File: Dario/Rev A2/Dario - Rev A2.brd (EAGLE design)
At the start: 55 x 30 mm, 31 parts, among them J1 1241050-5, J2 21_PIN, J3 21_PIN, SW1 KMR211G, U1 MK20DX256VLH7, Y1 8MHz, Y2 32.768kHz, 12.5pF

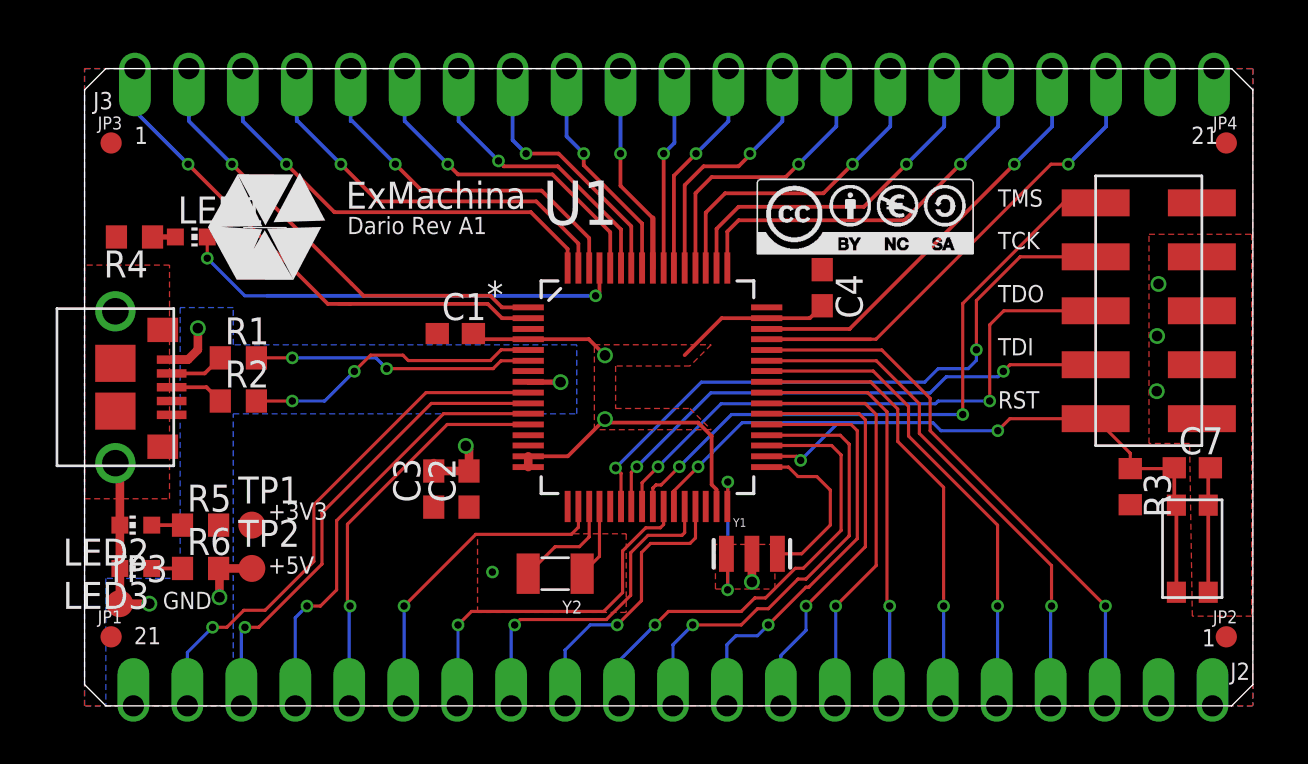
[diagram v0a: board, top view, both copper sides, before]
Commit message: Change the pin out of the jtag connector and change the width of all nets to 0.1778mm
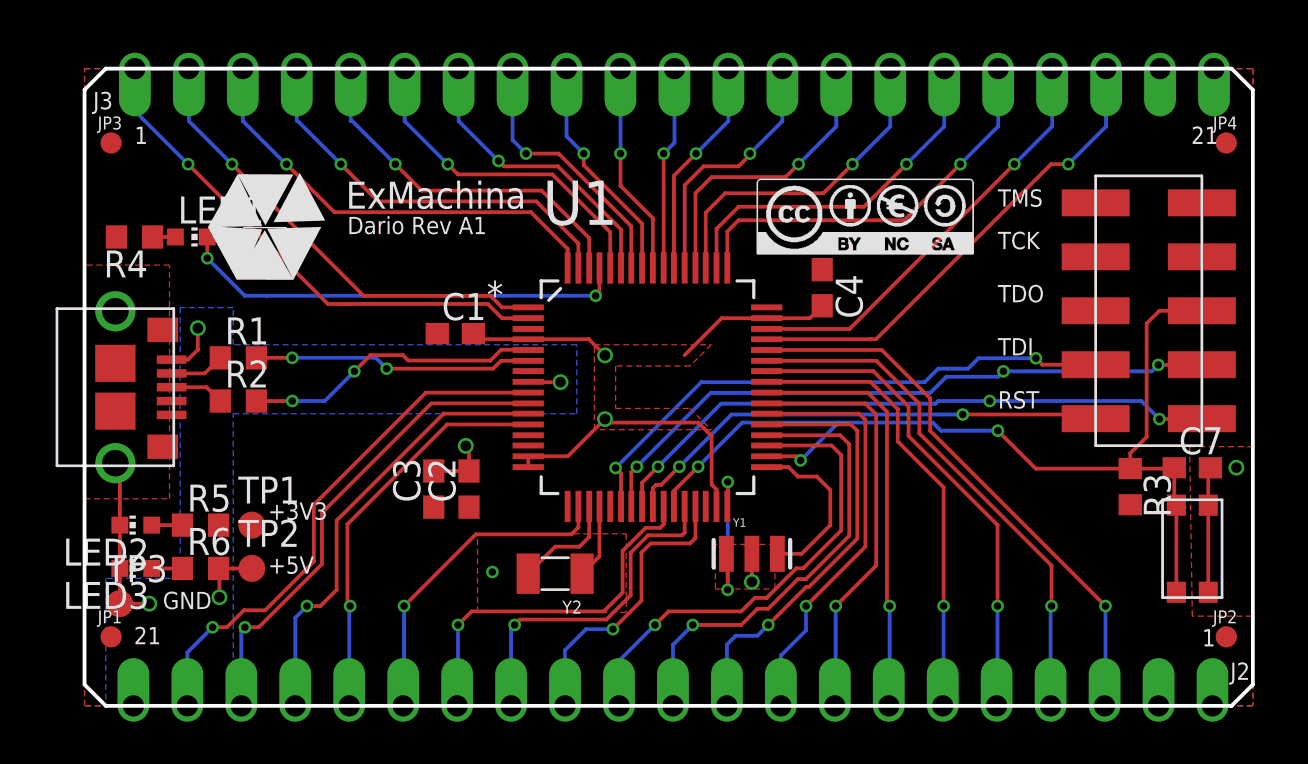
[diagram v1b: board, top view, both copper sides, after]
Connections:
- net GND: now also J1.2; no longer J1.3, J1.5, J1.7, J1.9
- net RESET: now also J1.5; no longer J1.10
- net TCK/SWDCLK: now also J1.8; no longer J1.4
- net TDI: now also J1.7; no longer J1.8
- net TDO: now also J1.9; no longer J1.6
- net TMS/SWDIO: now also J1.10; no longer J1.2
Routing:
- net RESET: track 37.5 -> 46.6 mm
- net TMS/SWDIO: track 30.4 -> 23.3 mm
- net TDI: track 25.6 -> 30.6 mm, vias 2 -> 3
- net TCK/SWDCLK: track 30.3 -> 26.8 mm
- net TDO: track 27.9 -> 29.4 mm, vias 2 -> 3
- net GND: vias 9 -> 7

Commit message: Enlarge the board to have a multiple of 0.1 inch
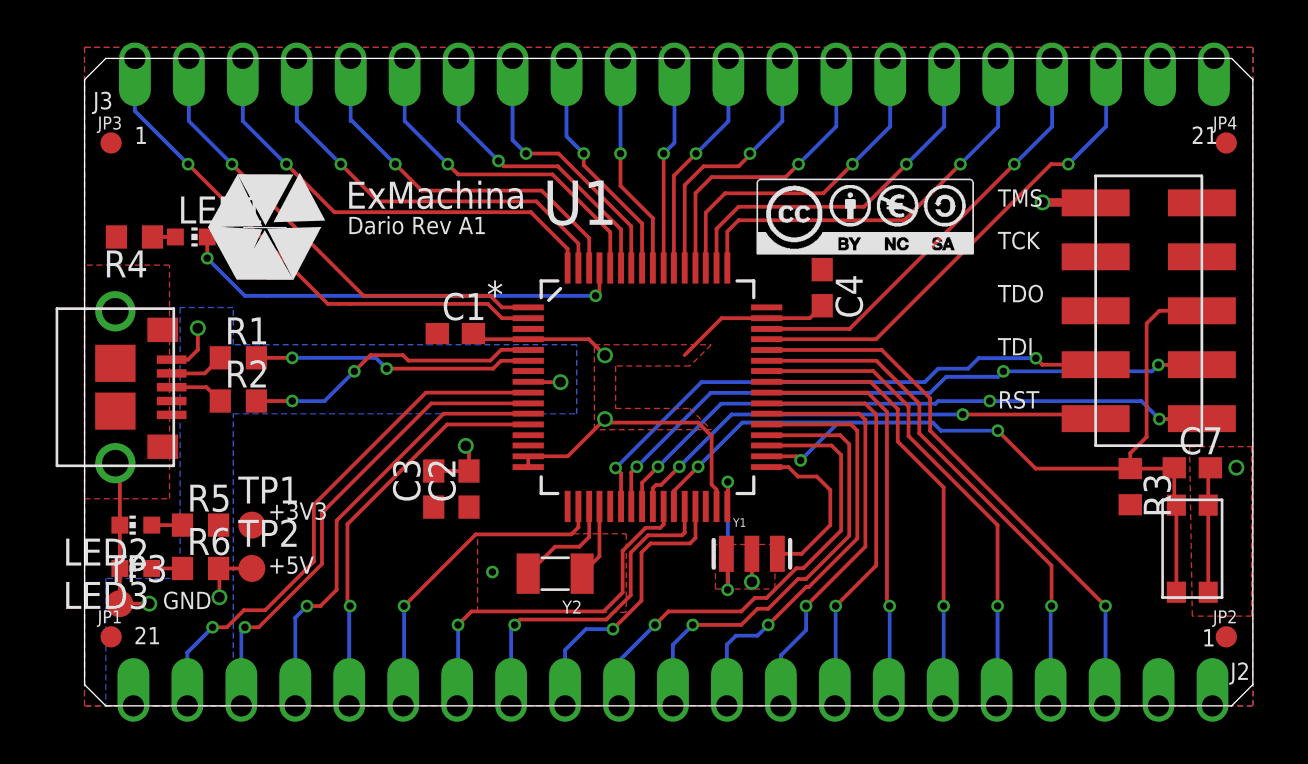
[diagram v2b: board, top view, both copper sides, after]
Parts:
- moved J3 0.48 mm to (27.8, 30.5)
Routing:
- net GND: track 46.3 -> 48.8 mm, vias 7 -> 8
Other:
- board size 55 x 30 mm -> 55 x 30.5 mm

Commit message: Rename the name on the board and add the name on some pin of JTAG connector
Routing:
- net TDO: vias 3 -> 2
- net TDI: vias 3 -> 2
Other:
- outline, holes or cut-outs redrawn
- board text removed: "RST"
- board text removed: "TDI"
- board text removed: "TDO"
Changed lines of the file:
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@@
 <setting verticaltext="up"/>
 </settings>
-<grid distance="0.1" unitdist="inch" unit="mm" style="lines" multiple="1" display="yes" altdistance="0.05" altunitdist="inch" altunit="mm"/>
+<grid distance="1.27" unitdist="mm" unit="mm" style="lines" multiple="1" display="yes" altdistance="0.635" altunitdist="mm" altunit="mm"/>
 <layers>
 <layer number="1" name="Top" color="4" fill="1" visible="yes" active="yes"/>
@@
 <wire x1="54" y1="30.48" x2="1" y2="30.48" width="0" layer="20"/>
 <wire x1="1" y1="30.48" x2="0" y2="29.48" width="0" layer="20"/>
-<wire x1="0" y1="29.48" x2="0" y2="29" width="0" layer="20"/>
-<wire x1="0" y1="29" x2="0" y2="1" width="0" layer="20"/>
+<wire x1="0" y1="29.48" x2="0" y2="1" width="0" layer="20"/>
 <wire x1="0" y1="1" x2="1" y2="0" width="0" layer="20"/>
 <wire x1="1" y1="0" x2="54" y2="0" width="0" layer="20"/>
@@
 <text x="0.402" y="28.086" size="0.8128" layer="21">J3</text>
 <text x="53.934" y="1.222" size="0.8128" layer="21">J2</text>
-<text x="43" y="14" size="0.8128" layer="21">RST</text>
-<text x="43" y="16.5" size="0.8128" layer="21">TDI</text>
-<text x="43" y="19" size="0.8128" layer="21">TDO</text>
-<text x="43" y="23.5" size="0.8128" layer="21">TMS</text>
-<text x="43" y="21.5" size="0.8128" layer="21">TCK</text>
+<text x="43" y="23.5" size="0.8128" layer="21">GND</text>
+<text x="41.73" y="15.785" size="0.8128" layer="21">TCK</text>
+<text x="41.73" y="13.975" size="0.8128" layer="21">TMS</text>
 </plain>
 <attributes>
@@
 <via x="19.2" y="6.3" extent="1-16" drill="0.35"/>
 <contactref element="J1" pad="2"/>
-<via x="45.1" y="23.7" extent="1-16" drill="0.5"/>
+<via x="50.18" y="23.7" extent="1-16" drill="0.5"/>
 <wire x1="47.6" y1="23.68" x2="47.58" y2="23.7" width="0.4064" layer="1"/>
-<wire x1="47.58" y1="23.7" x2="45.1" y2="23.7" width="0.4064" layer="1"/>
+<wire x1="47.58" y1="23.7" x2="50.18" y2="23.7" width="0.4064" layer="1"/>
 </signal>
 <signal name="+5V">
@@
 <wire x1="26.246" y1="9.3866" x2="26.246" y2="10.503" width="0.1778" layer="1"/>
 <wire x1="26.246" y1="10.503" x2="27" y2="11.257" width="0.1778" layer="1"/>
-<via x="42.612" y="14.351" extent="1-16" drill="0.35"/>
 <wire x1="29.967" y1="14.224" x2="40.061" y2="14.224" width="0.1778" layer="16"/>
 <wire x1="40.061" y1="14.224" x2="40.188" y2="14.351" width="0.1778" layer="16"/>
-<wire x1="40.188" y1="14.351" x2="42.612" y2="14.351" width="0.1778" layer="16"/>
 <wire x1="27" y1="11.257" x2="29.967" y2="14.224" width="0.1778" layer="16"/>
 <contactref element="J1" pad="9"/>
-<wire x1="42.612" y1="14.351" x2="49.749" y2="14.351" width="0.1778" layer="16"/>
+<wire x1="40.188" y1="14.351" x2="49.749" y2="14.351" width="0.1778" layer="16"/>
 <wire x1="49.749" y1="14.351" x2="50.6" y2="13.5" width="0.1778" layer="16"/>
 <via x="50.6" y="13.5" extent="1-16" drill="0.35"/>
@@
 <wire x1="29.475" y1="14.732" x2="39.807" y2="14.732" width="0.1778" layer="16"/>
 <wire x1="39.807" y1="14.732" x2="40.569" y2="15.494" width="0.1778" layer="16"/>
-<via x="43.255" y="15.748" extent="1-16" drill="0.35"/>
-<wire x1="43.255" y1="15.748" x2="43.001" y2="15.494" width="0.1778" layer="16"/>
-<wire x1="43.001" y1="15.494" x2="40.569" y2="15.494" width="0.1778" layer="16"/>
 <wire x1="26" y1="11.257" x2="29.475" y2="14.732" width="0.1778" layer="16"/>
 <contactref element="J1" pad="7"/>
-<wire x1="43.255" y1="15.748" x2="50.248" y2="15.748" width="0.1778" layer="16"/>
-<wire x1="50.248" y1="15.748" x2="50.55" y2="16.05" width="0.1778" layer="16"/>
 <via x="50.55" y="16.05" extent="1-16" drill="0.35"/>
 <wire x1="50.55" y1="16.05" x2="52.59" y2="16.05" width="0.1778" layer="1"/>
 <wire x1="52.59" y1="16.05" x2="52.6" y2="16.06" width="0.1778" layer="1"/>
+<wire x1="40.569" y1="15.494" x2="49.994" y2="15.494" width="0.1778" layer="16"/>
+<wire x1="49.994" y1="15.494" x2="50.55" y2="16.05" width="0.1778" layer="16"/>
 </signal>
 <signal name="TMS/SWDIO">

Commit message: Resize the board
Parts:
- moved J3 1.27 mm to (27.8, 29.2)
- moved JP3 0.64 mm to (1.25, 25.9)
- moved JP4 0.64 mm to (53.8, 25.9)
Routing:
- net PTD7: track 21.6 -> 20.4 mm
- net PTD3: track 16.5 -> 15.2 mm
- net PTE1: track 25.0 -> 23.8 mm
- net PTE0: track 22.6 -> 21.3 mm
- net PTD6: track 19.7 -> 18.5 mm
- net PTD2: track 14.5 -> 13.3 mm
- net PTD1: track 13.1 -> 11.8 mm
- net PTD0: track 11.3 -> 10.1 mm
- net PTC9: track 10.9 -> 9.66 mm
- net PTC8: track 12.7 -> 11.5 mm
- net PTC7: track 14.7 -> 13.4 mm
- net PTC6: track 16.2 -> 14.9 mm
- net PTC5: track 17.8 -> 16.5 mm
- net PTC4: track 19.7 -> 18.4 mm
- net PTC3: track 20.6 -> 19.3 mm
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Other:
- board size 55 x 30.5 mm -> 55 x 29.2 mm
- board text added: "Dario Rev A2"
- board text removed: "Dario Rev A1"
